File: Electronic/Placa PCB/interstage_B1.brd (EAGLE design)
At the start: 82.5 x 29 mm, 9 parts, among them J1 0532611271, J3 0532611271, Q1 PMV16XNR, U1 LM70CIMM-3, U2 LM70CIMM-3

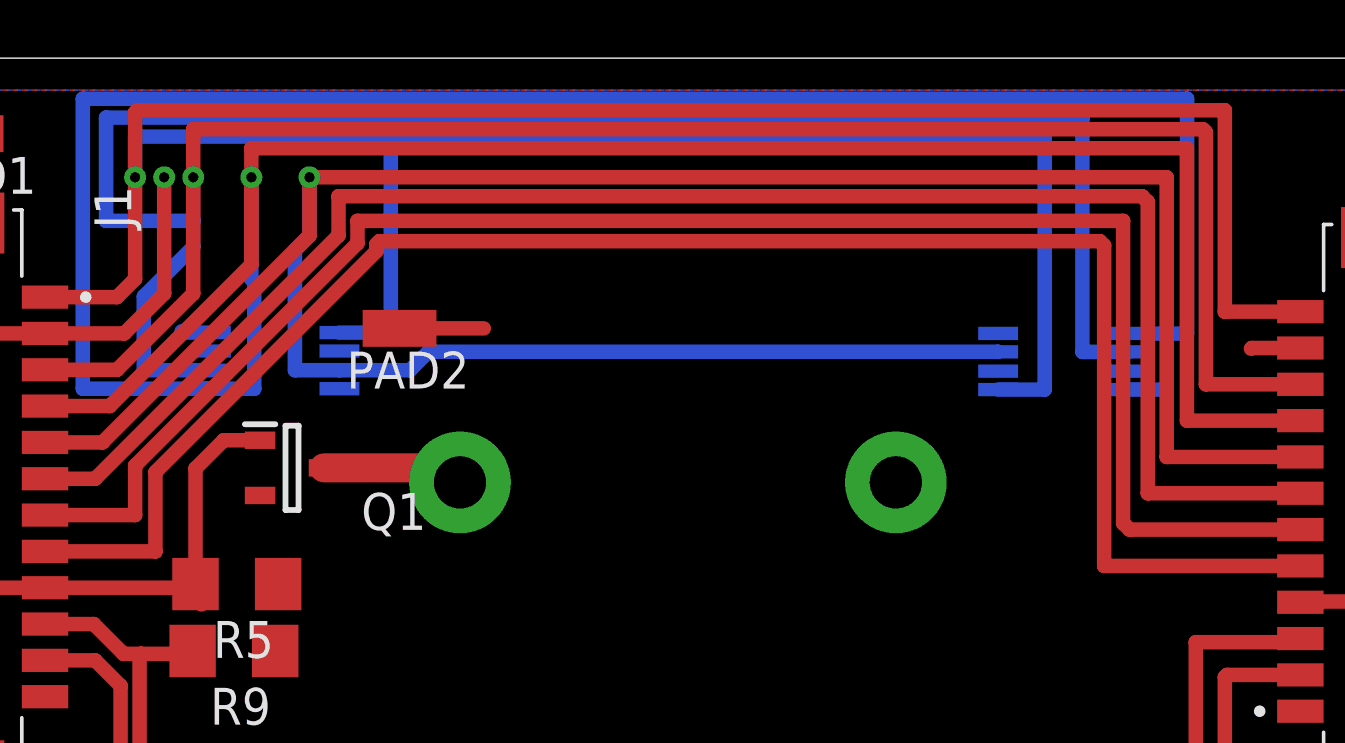
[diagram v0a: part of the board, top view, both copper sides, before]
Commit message: Ensamblaje placa
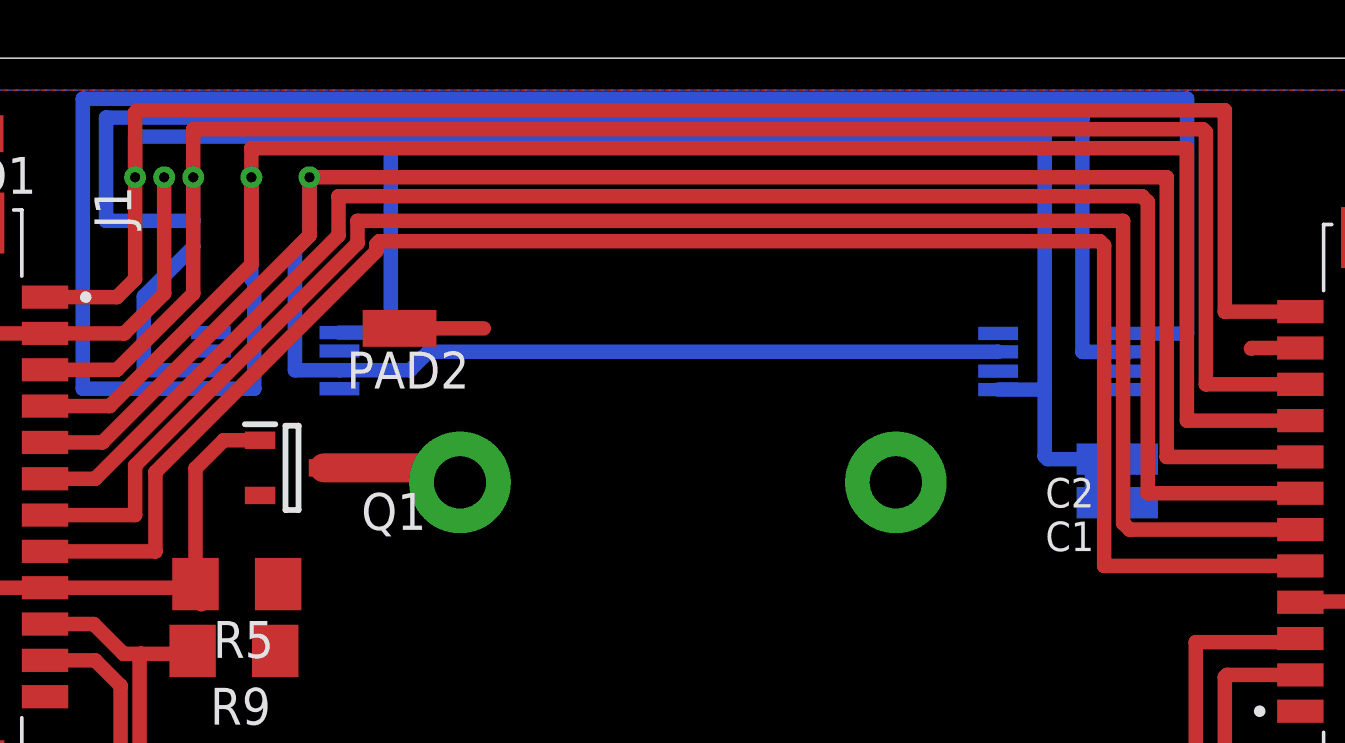
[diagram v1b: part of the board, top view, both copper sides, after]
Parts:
- added C1, C2: 0.1pF, rcl:C0603K
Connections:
- net GND: now also C1.2, C2.2
- net VCC: now also C1.1, C2.1
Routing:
- net VCC: track 107.7 -> 113.2 mm
- net GND: track 31.5 -> 29.2 mm
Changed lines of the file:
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@@
 <attribute name="VALUE" x="17.6" y="25.6" size="0.0254" layer="27" rot="R90"/>
+</element>
+<element name="C1" library="rcl" library_urn="urn:adsk.eagle:library:334" package="C0603K" package3d_urn="urn:adsk.eagle:package:23680/2" value="0.1pF" x="47.8" y="13.8" smashed="yes" rot="MR180">
+<attribute name="NAME" x="47" y="13.15" size="1.016" layer="25" rot="R180"/>
+<attribute name="SPICEPREFIX" value="C" x="47.8" y="13.8" size="1.778" layer="28" rot="MR180" display="off"/>
+<attribute name="VALUE" x="47" y="15.45" size="1.016" layer="27" rot="R180"/>
+</element>
+<element name="C2" library="rcl" library_urn="urn:adsk.eagle:library:334" package="C0603K" package3d_urn="urn:adsk.eagle:package:23680/2" value="0.1pF" x="47.8" y="15.3" smashed="yes" rot="MR180">
+<attribute name="NAME" x="47" y="14.65" size="1.016" layer="25" rot="R180"/>
+<attribute name="SPICEPREFIX" value="C" x="47.8" y="15.3" size="1.778" layer="28" rot="MR180" display="off"/>
+<attribute name="VALUE" x="47" y="16.95" size="1.016" layer="27" rot="R180"/>
 </element>
 </elements>
@@
 <contactref element="R5" pad="1"/>
 <contactref element="J1" pad="2"/>
-<contactref element="U2" pad="4"/>
 <polygon width="0.3" layer="1" spacing="0.3048">
 <vertex x="3.5" y="28"/>
@@
 <vertex x="61.5" y="28"/>
 </polygon>
-<contactref element="U1" pad="4"/>
 <polygon width="0.5" layer="16">
 <vertex x="3.6" y="28"/>
@@
 <wire x1="54.1" y1="19.125" x2="52.425" y2="19.125" width="0.5" layer="1"/>
 <wire x1="52.425" y1="19.125" x2="52.4" y2="19.1" width="0.5" layer="1"/>
-<wire x1="48.1198" y1="17.6948" x2="49.3948" y2="17.6948" width="0.5" layer="16"/>
-<wire x1="49.3948" y1="17.6948" x2="49.4" y2="17.7" width="0.5" layer="16"/>
-<wire x1="16.6102" y1="19.6552" x2="15.6448" y2="19.6552" width="0.5" layer="16"/>
-<wire x1="15.6448" y1="19.6552" x2="15.6" y2="19.7" width="0.5" layer="16"/>
-<wire x1="10.9" y1="19.625" x2="15.6" y2="19.7" width="0" layer="19" extent="1-16"/>
-<wire x1="49.4" y1="17.7" x2="52.4" y2="19.1" width="0" layer="19" extent="1-16"/>
+<contactref element="C2" pad="2"/>
+<contactref element="C1" pad="2"/>
+<contactref element="U1" pad="4"/>
+<contactref element="U2" pad="4"/>
+<wire x1="15" y1="25" x2="16.6102" y2="19.6552" width="0" layer="19" extent="16-16"/>
+<wire x1="48.1198" y1="17.6948" x2="52.4" y2="19.1" width="0" layer="19" extent="1-16"/>
 <wire x1="18.3" y1="14.05" x2="16.6102" y2="19.6552" width="0" layer="19" extent="1-16"/>
 </signal>
@@
 <signal name="VCC">
 <contactref element="J1" pad="1"/>
-<contactref element="U2" pad="5"/>
-<contactref element="U1" pad="5"/>
 <contactref element="J3" pad="12"/>
 <via x="14" y="25" extent="1-16" drill="0.35"/>
@@
 <wire x1="13.375" y1="20.875" x2="14" y2="21.5" width="0.5" layer="1"/>
 <wire x1="14" y1="21.5" x2="14" y2="25" width="0.5" layer="1"/>
-<wire x1="21.0298" y1="19.6552" x2="22.8" y2="19.6552" width="0.5" layer="16"/>
 <wire x1="22.8" y1="19.6552" x2="22.8" y2="26.3" width="0.5" layer="16"/>
 <wire x1="22.8" y1="26.3" x2="22.7" y2="26.4" width="0.5" layer="16"/>
@@
 <wire x1="22.7" y1="26.4" x2="14" y2="26.4" width="0.5" layer="16"/>
 <wire x1="22.7" y1="26.4" x2="45.3" y2="26.4" width="0.5" layer="16"/>
-<wire x1="45.3" y1="17.6948" x2="43.7002" y2="17.6948" width="0.5" layer="16"/>
-<wire x1="45.3" y1="26.4" x2="45.3" y2="17.6948" width="0.5" layer="16"/>
+<wire x1="45.3" y1="17.6948" x2="45.3" y2="26.4" width="0.5" layer="16"/>
 <wire x1="51.4952" y1="27.3048" x2="51.5" y2="27.3" width="0.5" layer="1"/>
 <wire x1="51.5" y1="27.3" x2="51.5" y2="20.375" width="0.5" layer="1"/>
+<contactref element="C1" pad="1"/>
+<contactref element="C2" pad="1"/>
+<contactref element="U1" pad="5"/>
+<contactref element="U2" pad="5"/>
+<wire x1="21.0298" y1="19.6552" x2="22.8" y2="19.6552" width="0.5" layer="16"/>
+<wire x1="43.7002" y1="17.6948" x2="45.3" y2="17.6948" width="0.5" layer="16"/>
+<wire x1="46.925" y1="15.3" x2="46.925" y2="13.8" width="0.5" layer="16"/>
+<wire x1="45.3" y1="17.6948" x2="45.3" y2="15.4" width="0.5" layer="16"/>
+<wire x1="45.3" y1="15.4" x2="45.4" y2="15.3" width="0.5" layer="16"/>
+<wire x1="45.4" y1="15.3" x2="46.925" y2="15.3" width="0.5" layer="16"/>
 </signal>
 <signal name="T1">
